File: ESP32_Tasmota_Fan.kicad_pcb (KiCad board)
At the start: 2 copper layers, 70 x 45 mm, 45 parts, among them IC1 XL1509-ADJE1, J1 Conn_01x02_Female, J2 Conn_01x06, Q1 Q_PMOS_GDS, Q2 Q_PMOS_GDS, Q3 Q_PMOS_GDS, Q4 Q_PMOS_GDS, U1 DS18B20, U2 esp32-s2-wroom

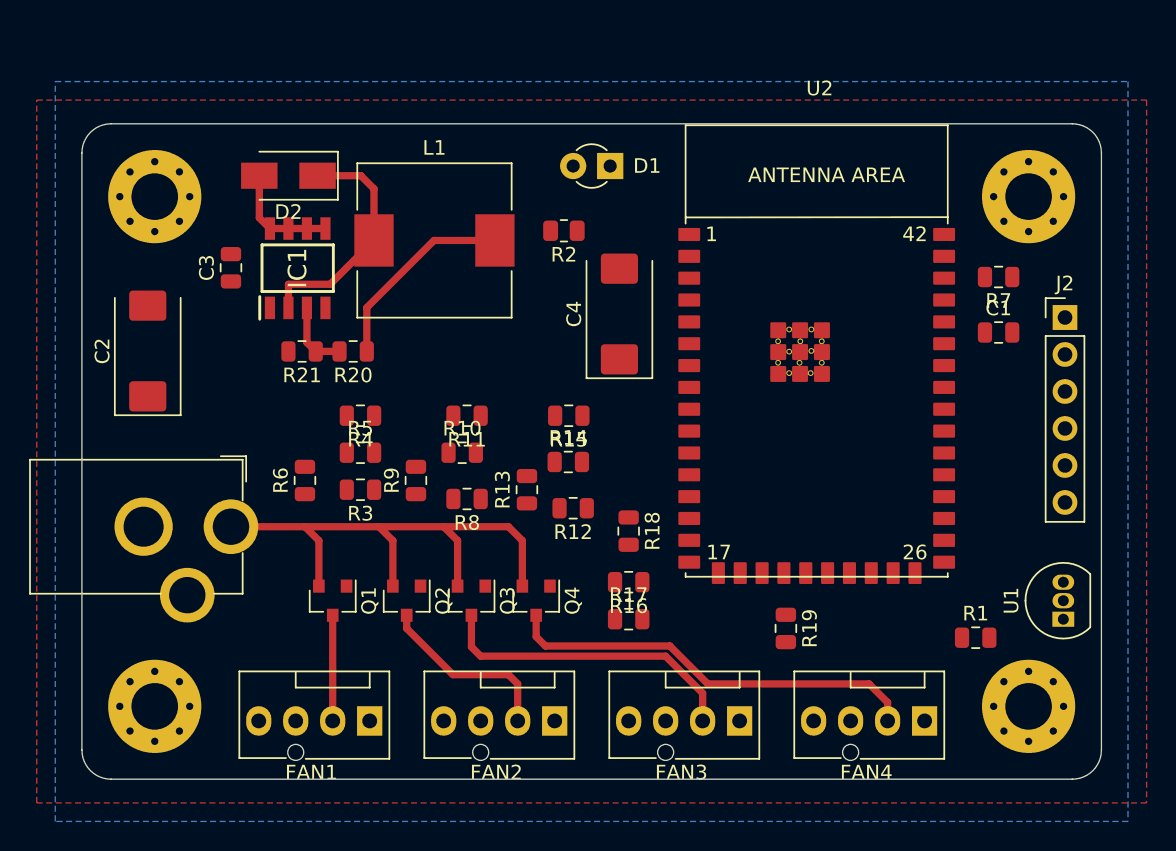
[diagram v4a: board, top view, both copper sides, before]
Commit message: First iteration with new ES32 - but not S2
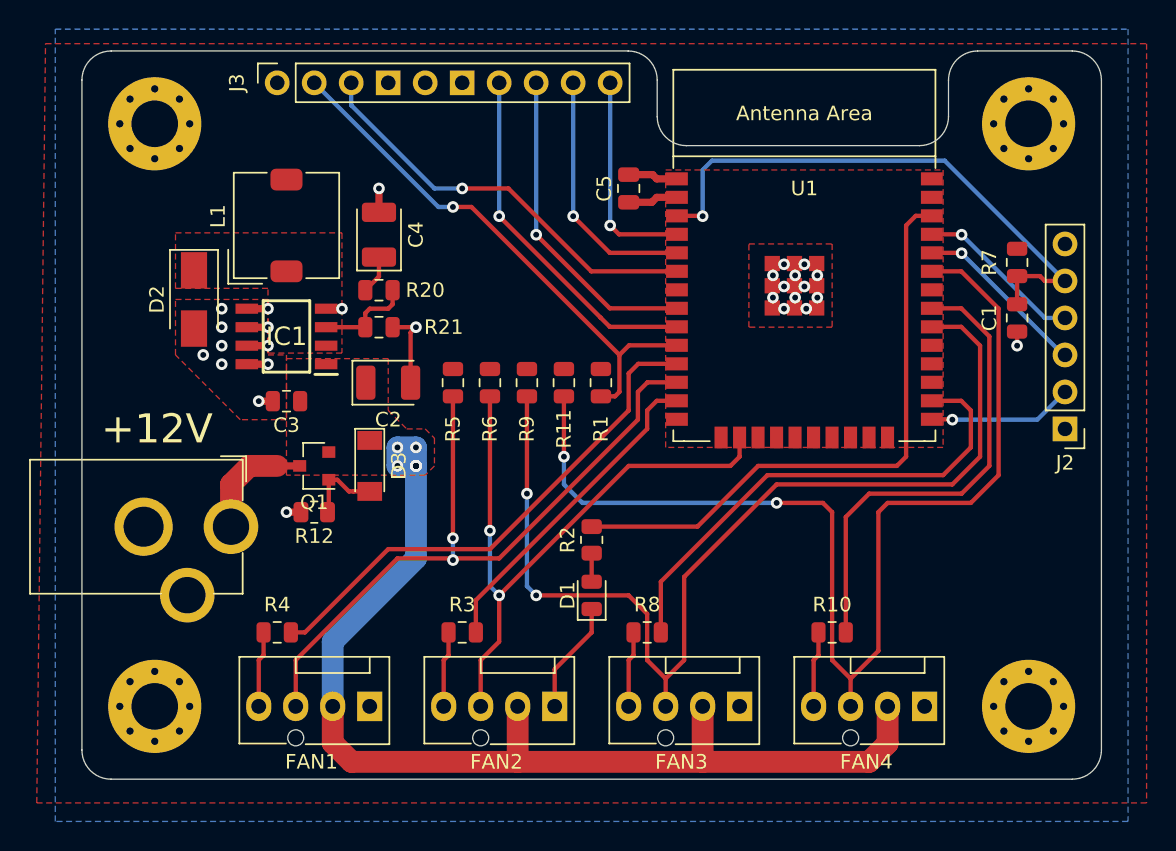
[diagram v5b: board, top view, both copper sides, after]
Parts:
- removed Q2, Q3, Q4: Q_PMOS_GDS, Package_TO_SOT_SMD:SOT-23
- removed R13, R14, R15, R16, R17, R18, R19: 10k, Resistor_SMD:R_0805_2012Metric
- removed U2: esp32-s2-wroom, ESP32-S2:esp32-s2-wrooom
- added C5: 1uF, Capacitor_SMD:C_0805_2012Metric, F.Cu at (121.9, 108.4)
- added D3: ZMM5V6, Diode_SMD:D_MiniMELF, F.Cu at (104.1, 127.4)
- added J3: Conn_01x10, Connector_PinSocket_2.54mm:PinSocket_1x10_P2.54mm_Vertical, F.Cu at (97.8, 101.1)
- C1: value C_Small -> 1uF/10V
- C2, C4: value CP -> 330uF/6.3V; footprint Capacitor_Tantalum_SMD:CP_EIA-7343-30_AVX-N -> Capacitor_Tantalum_SMD:CP_EIA-3528-15_AVX-H
- C3: value C_Small -> 1uF
- D1: footprint LED_THT:LED_D3.0mm -> LED_SMD:LED_0805_2012Metric
- L1: value INDUCTOR -> 33uH; footprint Inductor_SMD:L_10.4x10.4_H4.8 -> Inductor_SMD:L_TDK_SLF7045
- Q1: value Q_PMOS_GDS -> AO3401A
- R10, R12, R3, R4, R8: value 10k -> 100R
- R7: value R_Small -> 10k
- U1: value DS18B20 -> ESP32-WROOM-E; footprint Package_TO_SOT_THT:TO-92_Inline -> espressif:ESP32-WROOM-32E
- moved R1 31.1 mm to (120.0, 121.7), turned to 270 degrees
- moved D1 29.5 mm to (119.4, 136.3), turned to 90 degrees
- moved U1 29.2 mm to (134.0, 114.7), turned to 0 degrees
- moved R10 28.2 mm to (135.9, 138.8), turned to 180 degrees
- moved R2 21.3 mm to (119.4, 132.5), turned to 270 degrees
- moved R12 17.8 mm to (100.3, 130.6)
- moved C4 17.4 mm to (104.8, 111.5)
- moved C2 16.7 mm to (105.4, 121.7), turned to 0 degrees
- moved R4 15.9 mm to (97.8, 138.8)
- moved R8 15.4 mm to (123.2, 138.8)
- moved R6 14.4 mm to (112.4, 121.7), turned to 270 degrees
- moved R3 12.0 mm to (110.5, 138.8)
- moved D2 10.7 mm to (92.1, 116.0), turned to 270 degrees
- moved L1 10.2 mm to (98.4, 110.9), turned to 90 degrees
- moved R9 10.2 mm to (114.9, 121.7), turned to 270 degrees
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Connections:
- FAN1 pad 2: /FAN 1/SPLY -> +12V
- FAN1 pad 3: /FAN 1/SENSE -> /SENSE1
- FAN2 pad 2: /sheet6191C4D9/SPLY -> +12V
- FAN2 pad 3: /sheet6191C4D9/SENSE -> /SENSE2
- FAN2 pad 4: /sheet6191C4D9/PWM_Ctrl -> /sheet619566BF/PWM_Ctrl
- FAN3 pad 2: /sheet6191C6A1/SPLY -> +12V
- FAN3 pad 3: /sheet6191C6A1/SENSE -> /SENSE3
- FAN3 pad 4: /sheet6191C6A1/PWM_Ctrl -> /sheet61957927/PWM_Ctrl
- FAN4 pad 2: /sheet6191C855/SPLY -> +12V
- FAN4 pad 3: /sheet6191C855/SENSE -> /SENSE4
- FAN4 pad 4: /sheet6191C855/PWM_Ctrl -> /sheet61958B6B/PWM_Ctrl
- J1 pad 1: +12V -> /VIN
- J2 pad 2: /ESP32 Core/EN -> /ESP32 Core/IO0
- J2 pad 3: /ESP32 Core/IO0 -> /ESP32 Core/RX
- J2 pad 4: /ESP32 Core/RX -> /ESP32 Core/TX
- J2 pad 5: /ESP32 Core/TX -> /ESP32 Core/EN
- Q1 pad 1: Net-(Q1-Pad1) -> Net-(D3-Pad2)
- Q1 pad 3: /FAN 1/SPLY -> /VIN
- R1 pad 2: Net-(R1-Pad2) -> /OneWire
- R10 pad 1: +3V3 -> /PWM4
- R10 pad 2: /sheet6191C4D9/SENSE -> /sheet61958B6B/PWM_Ctrl
- R11 pad 1: /sheet6191C4D9/PWM -> +3V3
- R11 pad 2: /sheet6191C4D9/PWM_Ctrl -> /SENSE4
- R12 pad 1: /sheet6191C6A1/SW -> Net-(D3-Pad2)
- R12 pad 2: Net-(Q3-Pad1) -> GND
- R2 pad 1: LINK -> /LINK
- R3 pad 1: /FAN 1/SW -> /PWM2
- R3 pad 2: Net-(Q1-Pad1) -> /sheet619566BF/PWM_Ctrl
- R4 pad 1: /FAN 1/PWM -> /PWM1
- R5 pad 2: /FAN 1/SENSE -> /SENSE1
- R6 pad 1: Net-(Q1-Pad1) -> +3V3
- R6 pad 2: +3V3 -> /SENSE2
- R8 pad 1: /sheet6191C4D9/SW -> /PWM3
- R8 pad 2: Net-(Q2-Pad1) -> /sheet61957927/PWM_Ctrl
- R9 pad 1: Net-(Q2-Pad1) -> +3V3
- R9 pad 2: +3V3 -> /SENSE3
- U1 pad 2: Net-(R1-Pad2) -> +3V3
- U1 pad 3: +3V3 -> /ESP32 Core/EN
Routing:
- net /SENSE4: track 0.00 -> 77.7 mm, vias 0 -> 2
- net /SENSE3: track 0.00 -> 71.7 mm, vias 0 -> 2
- net /SENSE1: track 0.00 -> 49.6 mm, vias 0 -> 2
- net /SENSE2: track 0.00 -> 43.8 mm, vias 0 -> 2
- net /LINK: track 0.00 -> 41.5 mm
- net +12V: track 37.0 -> 76.4 mm, vias 0 -> 9
- net /ESP32 Core/EN: track 0.00 -> 39.3 mm, vias 0 -> 1
- net /OneWire: track 0.00 -> 36.9 mm, vias 0 -> 1
- net /PWM1: track 0.00 -> 35.6 mm
- net /PWM3: track 0.00 -> 34.1 mm
- net /PWM4: track 0.00 -> 32.9 mm
- net /sheet6191C855/SPLY: track 28.7 -> 0.00 mm
- net /EXT1: track 0.00 -> 28.6 mm, vias 0 -> 1
- net /SCL: track 0.00 -> 24.5 mm, vias 0 -> 1
- net /PWM2: track 0.00 -> 22.4 mm
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- added copper zone on F.Cu, net +12V
- added copper zone on F.Cu, net /DC/DC Buck/OUTPUT
- added copper zone on F.Cu, net GND
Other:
- board size 70 x 45 mm -> 70 x 50 mm
- board text added: "+12V"
- board text added: "+3V3"
- board text added: "1-W"
- board text added: "3V3"
- board text added: "BME280"
- board text added: "DHT-22"
- board text added: "DS18B20"
- board text added: "EN"
- board text added: "GND"
- board text added: "IO0"
- board text added: "IO34"
- board text added: "IO36"
- board text added: "IO39"
- board text added: "RX"
- board text added: "SCL"
- board text added: "SDA"
- board text added: "TX"

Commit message: Add JLC template
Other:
- board text added: "JLCJLCJLCJLC"
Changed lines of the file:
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@@
   (general
     (thickness 1.6)
-    (drawings 100)
+    (drawings 101)
     (tracks 268)
     (zones 0)
@@
     )
   )
+  (gr_text JLCJLCJLCJLC (at 109.22 103.285) (layer F.SilkS)
+    (effects (font (size 1 1) (thickness 0.15)))
+  )
   (gr_text +12V (at 89.535 124.875) (layer F.SilkS)

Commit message: Version open for review
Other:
- board text added: "ESP32 Fancontroller"
- board text added: "by zeroflow"
